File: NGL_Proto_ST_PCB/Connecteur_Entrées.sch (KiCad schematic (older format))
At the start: 9 parts, among them J1 Conn_01x08_Male, J3 227161-2

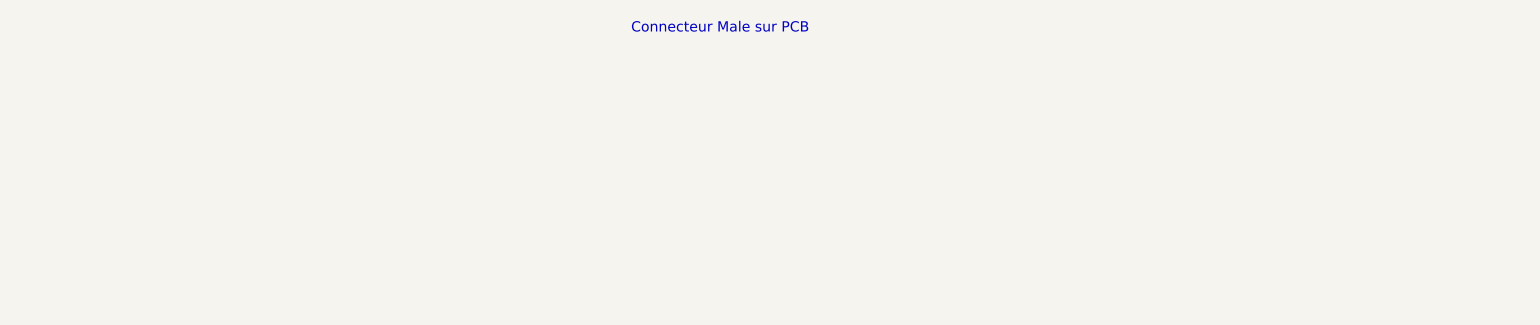
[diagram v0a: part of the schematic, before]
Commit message: Rrecherche sur pot num et mise en page
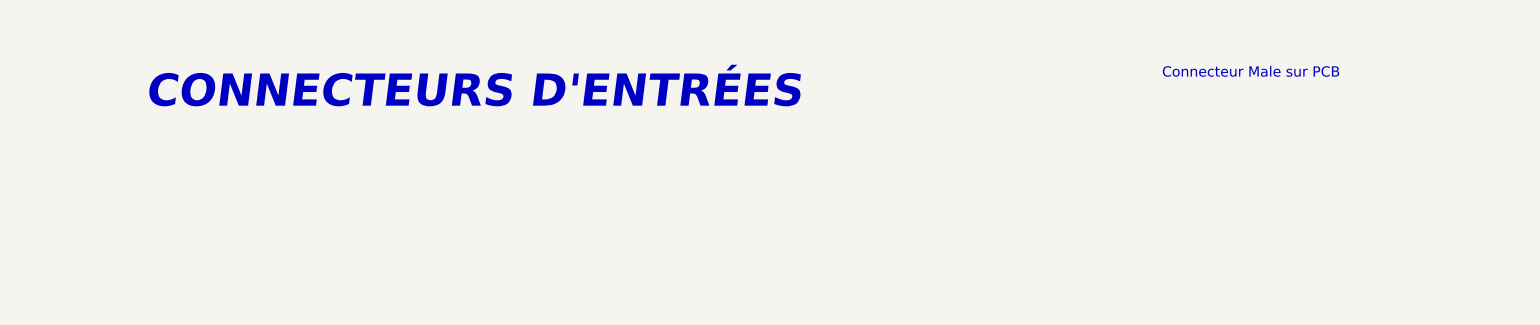
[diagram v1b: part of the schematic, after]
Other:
- note added: "CONNECTEURS D'ENTRÉES"
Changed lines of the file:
@@
 $Descr A4 11693 8268
 encoding utf-8
-Sheet 4 5
-Title "NGL_Proto"
-Date "2022-05-02"
-Rev "V1"
+Sheet 4 6
+Title "NGL_Proto_V2"
+Date "2022-05-27"
+Rev "V2"
 Comp "ADTP"
-Comment1 "Usinage by LPKF !"
-Comment2 ""
-Comment3 ""
+Comment1 "Auteur: Benoît"
+Comment2 "Proto avec potar numérique + intégration"
+Comment3 "Sous traité chez JLCPCB"
 Comment4 ""
 $EndDescr
@@
 	3015 3935 1790 3935
 $Bitmap
-Pos 7290 1470
+Pos 9880 1690
 Scale 2.000000
 Data
@@
 EndData
 $EndBitmap
-Text Notes 6570 845  0    50   ~ 0
+Text Notes 9160 1065 0    50   ~ 0
 Connecteur Male sur PCB
 Text GLabel 5205 3935 2    50   Output ~ 0
@@
 	1    0    0    -1
 $EndComp
+Text Notes 4200 1220 0    157  Italic 31
+CONNECTEURS D'ENTRÉES
 $EndSCHEMATC

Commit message: Commit avant DSN
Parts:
- C18: footprint Capacitor_SMD:C_0805_2012Metric -> Capacitor_SMD:C_0805_2012Metric_Pad1.18x1.45mm_HandSolder
- R11, R14, R3: footprint Resistor_SMD:R_0805_2012Metric -> Resistor_SMD:R_0805_2012Metric_Pad1.20x1.40mm_HandSolder
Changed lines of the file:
@@
 encoding utf-8
 Sheet 4 6
-Title "NGL_Proto_V2"
-Date "2022-05-27"
-Rev "V2"
+Title "NGL_Proto_ST"
+Date "2022-06-09"
+Rev "V1.1"
 Comp "ADTP"
 Comment1 "Auteur: Benoît"
@@
 F 0 "R3" H 3235 3981 50  0000 L CNN
 F 1 "127K" H 3235 3890 50  0000 L CNN
-F 2 "Resistor_SMD:R_0805_2012Metric" V 3095 3935 50  0001 C CNN
+F 2 "Resistor_SMD:R_0805_2012Metric_Pad1.20x1.40mm_HandSolder" V 3095 3935 50  0001 C CNN
 F 3 "~" H 3165 3935 50  0001 C CNN
 	1    3165 3935
@@
 F 0 "R14" H 4710 3981 50  0000 L CNN
 F 1 "1K" H 4710 3890 50  0000 L CNN
-F 2 "Resistor_SMD:R_0805_2012Metric" V 4570 3935 50  0001 C CNN
+F 2 "Resistor_SMD:R_0805_2012Metric_Pad1.20x1.40mm_HandSolder" V 4570 3935 50  0001 C CNN
 F 3 "~" H 4640 3935 50  0001 C CNN
 	1    4640 3935
@@
 F 0 "C18" H 10115 5556 50  0000 L CNN
 F 1 "1nF" H 10115 5465 50  0000 L CNN
-F 2 "Capacitor_SMD:C_0805_2012Metric" H 10038 5360 50  0001 C CNN
+F 2 "Capacitor_SMD:C_0805_2012Metric_Pad1.18x1.45mm_HandSolder" H 10038 5360 50  0001 C CNN
 F 3 "" H 10000 5510 50  0001 C CNN
 	1    10000 5510
@@
 F 0 "R11" H 9645 5546 50  0000 L CNN
 F 1 "10K" H 9645 5455 50  0000 L CNN
-F 2 "Resistor_SMD:R_0805_2012Metric" V 9505 5500 50  0001 C CNN
+F 2 "Resistor_SMD:R_0805_2012Metric_Pad1.20x1.40mm_HandSolder" V 9505 5500 50  0001 C CNN
 F 3 "~" H 9575 5500 50  0001 C CNN
 	1    9575 5500
